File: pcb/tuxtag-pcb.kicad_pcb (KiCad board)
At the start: 2 copper layers, 25.8 x 37.2 mm, 13 parts, among them J1 vibrator, J2 battery, J3 buzzer, Q1 P2N2222A, U1 ESP32-C3_SUPERMINI_TH

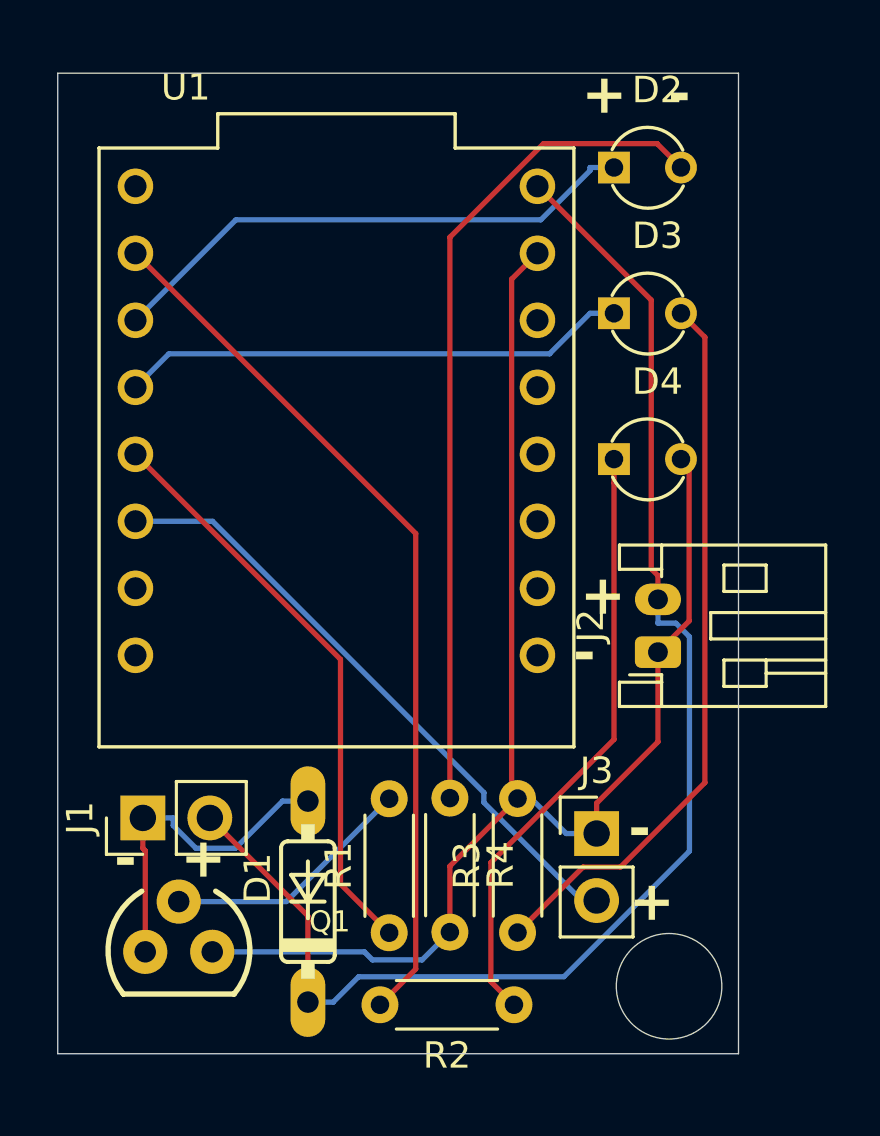
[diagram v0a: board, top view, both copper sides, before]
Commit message: Updated PCB design with vias as per manufacturer request
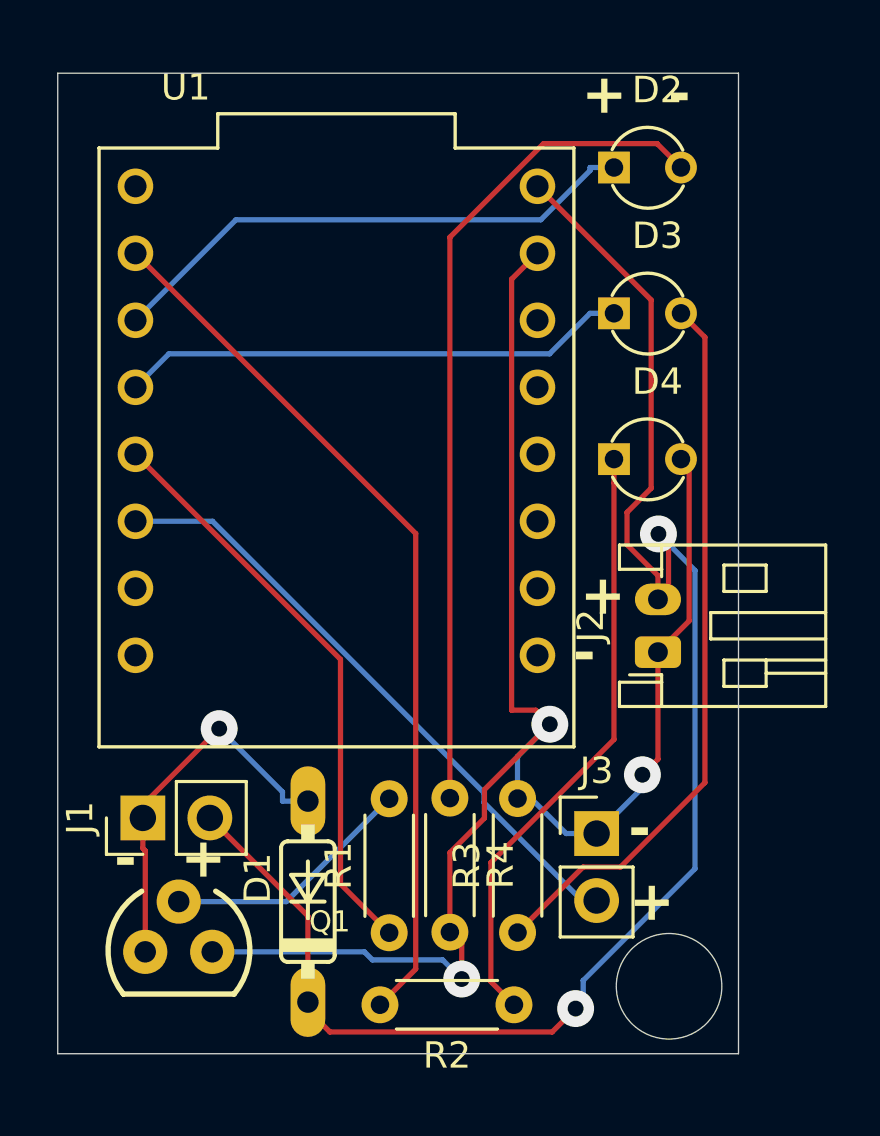
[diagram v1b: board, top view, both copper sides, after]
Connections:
- D1 pad A: Net-(J1-Pin_1) -> (no net)
- D1 pad C: Net-(J1-Pin_2) -> (no net)
- D2 pad A: Net-(U1-GPIO7) -> (no net)
- D2 pad C: Net-(D2-PadC) -> (no net)
- D3 pad A: Net-(U1-GPIO8) -> (no net)
- D3 pad C: Net-(D3-PadC) -> (no net)
- D4 pad A: Net-(D4-PadA) -> (no net)
- D4 pad C: Net-(J2-Pin_1) -> (no net)
- J1 pad 1: Net-(J1-Pin_1) -> (no net)
- J1 pad 2: Net-(J1-Pin_2) -> (no net)
- J2 pad 1: Net-(J2-Pin_1) -> (no net)
- J2 pad 2: Net-(J1-Pin_2) -> (no net)
- J3 pad 1: Net-(J2-Pin_1) -> (no net)
- J3 pad 2: Net-(J3-Pin_2) -> (no net)
- Q1 pad 1: Net-(J2-Pin_1) -> (no net)
- Q1 pad 2: Net-(Q1-Pad2) -> (no net)
- Q1 pad 3: Net-(J1-Pin_1) -> (no net)
- R1 pad 1: Net-(U1-GPIO9) -> (no net)
- R1 pad 2: Net-(Q1-Pad2) -> (no net)
- R2 pad 1: Net-(D4-PadA) -> (no net)
- R2 pad 2: Net-(U1-GPIO6) -> (no net)
- R3 pad 1: Net-(D3-PadC) -> (no net)
- R3 pad 2: Net-(J2-Pin_1) -> (no net)
- R4 pad 1: Net-(D2-PadC) -> (no net)
- R4 pad 2: Net-(J2-Pin_1) -> (no net)
- U1 pad 10: Net-(J3-Pin_2) -> (no net)
- U1 pad 5V: Net-(J1-Pin_2) -> (no net)
- U1 pad 6: Net-(U1-GPIO6) -> (no net)
- U1 pad 7: Net-(U1-GPIO7) -> (no net)
- U1 pad 8: Net-(U1-GPIO8) -> (no net)
- U1 pad 9: Net-(U1-GPIO9) -> (no net)
- U1 pad G: Net-(J2-Pin_1) -> (no net)
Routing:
- net (no net): track 0.00 -> 350.5 mm, vias 0 -> 6
- net Net-(J2-Pin_1): track 56.2 -> 0.00 mm
- net Net-(J1-Pin_2): track 53.3 -> 0.00 mm
- net Net-(U1-GPIO6): track 33.5 -> 0.00 mm
- net Net-(D2-PadC): track 31.9 -> 0.00 mm
- net Net-(D3-PadC): track 27.6 -> 0.00 mm
- net Net-(J3-Pin_2): track 23.7 -> 0.00 mm
- net Net-(D4-PadA): track 23.0 -> 0.00 mm
- net Net-(U1-GPIO9): track 22.1 -> 0.00 mm
- net Net-(U1-GPIO7): track 20.6 -> 0.00 mm
- net Net-(U1-GPIO8): track 19.3 -> 0.00 mm
- net Net-(J1-Pin_1): track 12.8 -> 0.00 mm
- net Net-(Q1-Pad2): track 9.59 -> 0.00 mm
